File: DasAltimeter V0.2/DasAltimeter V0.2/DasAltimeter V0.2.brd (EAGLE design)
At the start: 38.9 x 21.6 mm, 53 parts, among them IC1 BMI055, U1 ATSAMD21G-A, U2 3.3V/150mA, U3 MS5803-14BA, U4 ADXL193, X1 22-23-2041, X2 22-23-2041

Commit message: playing with mini altimeter idea
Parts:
- removed C9: 0.1uF, SparkFun-Capacitors:0402
- removed H1: STAND-OFFTIGHT, SparkFun-Hardware:STAND-OFF-TIGHT
- removed R10, R14: 27k, SparkFun-Resistors:0402
- removed R11, R7: 100, SparkFun-Resistors:0402
- removed R12, R8: 3.3k, SparkFun-Resistors:0402
- removed R13, R9: 100k, SparkFun-Resistors:0402
- removed U$3: SI7232DN, SaL-lib1:SI7232DN
- removed U1: ATSAMD21G-A, SparkFun-IC-Microcontroller:TQFP-48
- removed U3: MS5803-14BA, SparkFun-Sensors:MS5803
- removed U4: ADXL193, SparkFun-Sensors:LCC-8
- removed X1: 22-23-2041, con-molex:22-23-2041
- added U$2: ATSAMD10D, SaL-lib1:ATSAMD10D
- added U$5: SIMPLE-MS5607, MS5607:MS5607
- C3: value 0.1uF -> 100nF
- C5: value 0.1uF -> 4.7uF
- moved X2 25.8 mm to (10.9, -7.49), turned to 0 degrees
- moved R2 24.8 mm to (21.2, -9.14), flipped to the bottom
- moved D2 22.8 mm to (22.9, -8.13)
- moved R17 22.2 mm to (13.8, -5.33), turned to 0 degrees
- moved R21 22.0 mm to (8.08, -5.33), turned to 0 degrees
- moved R4 21.7 mm to (24.1, -2.79), flipped to the bottom, turned to 0 degrees
- moved MEM 21.0 mm to (25.8, -3.05), turned to 0 degrees
- moved R5 20.8 mm to (26.5, 0.76), turned to 90 degrees
- moved C1 20.1 mm to (6.10, 2.16)
- moved C2 19.7 mm to (10.9, 2.03)
- moved U2 19.5 mm to (8.51, 2.16)
- moved C4 19.5 mm to (19.1, -3.81), turned to 0 degrees
- moved R18 19.4 mm to (13.8, -3.81), turned to 180 degrees
- moved R22 19.2 mm to (8.08, -3.81), turned to 180 degrees
- moved C8 18.6 mm to (33.4, -3.30)
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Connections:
- removed net FET_C: R9.1, U$3.7, U$3.8, U$3.9, X1.2
- removed net FET_D: R13.2, U$3.10, U$3.5, U$3.6, X1.3
- removed net FIRE_C: R7.2, R8.1, U1.34
- removed net FIRE_D: R11.1, R12.2, U1.33
- removed net N$3: C4.1, U1.43
- removed net N$8: R11.2, U$3.4
- removed net SENSE_C: R10.1, R9.2, U1.4
- removed net SENSE_D: R13.1, R14.2, U1.3
- removed net SPI0_MISO: IC1.10, IC1.15, U1.16
- removed net SPI0_MOSI: IC1.9, U1.13
- removed net SPI0_SCK: IC1.8, U1.14
- removed net SPI2_MISO: U1.22, U3.8
- removed net SPI2_MOSI: U1.21, U3.7
- removed net SPI2_SCK: U1.24, U3.1
- net !RESET: now also U$2.18; no longer U1.40
- net 3.3V: now also C4.1; no longer C3.1, C9.1, U1.17, U1.36, U1.44, U3.5, U4.P$7, U4.P$8
- net ACCELX: now also U$2.6; no longer U1.12, U4.P$6
- net BUZZER: now also U$2.10; no longer U1.30
- net CS_ACCEL: now also U$2.11; no longer U1.19
- net CS_BARO: now also U$2.17, U$5.5; no longer U1.23, U3.3
- net CS_GYRO: now also U$2.12; no longer U1.15
- net CS_MEM: now also U$2.13; no longer U1.27
- net FIRE_A: now also U$2.8; no longer U1.38
- net FIRE_B: now also U$2.7; no longer U1.37
- net GND: now also U$2.23, U$5.3; no longer C4.2, C9.2, R10.2, R12.1, R14.1, R8.2, U$3.1, U$3.3, U1.18, U1.35, U1.42, U1.5, U3.2, U3.6, U4.P$3
- net LED: now also U$2.9; no longer U1.29
- net N$1: now also C4.2, U$5.1; no longer R7.1, U$3.2
- net N$4: now also C3.1, U$2.24; no longer U1.6
- net RX: now also U$2.22; no longer U1.32
- net SENSE_A: now also U$2.1; no longer U1.48
- net SENSE_B: now also U$2.2; no longer U1.47
- net SENSE_BAT: now also U$2.5; no longer U1.11
- net SPI1_MISO: now also IC1.10, IC1.15, U$2.14; no longer U1.28
- net SPI1_MOSI: now also IC1.9, U$2.15; no longer U1.25
- net SPI1_SCK: now also IC1.8, U$2.16; no longer U1.26
- net SWCLK: now also U$2.19; no longer U1.45
- net SWDIO: now also U$2.20; no longer U1.46
- net TX: now also U$2.21; no longer U1.31
- net VCC: no longer X1.1, X1.4
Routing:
- net FIRE_A: track 19.4 -> 0.00 mm, vias 2 -> 0
- net 3.3V: track 15.8 -> 0.00 mm
- net CS_BARO: track 14.7 -> 0.00 mm
- net CS_MEM: track 14.4 -> 0.00 mm, vias 2 -> 0
- net LED: track 14.3 -> 0.00 mm, vias 1 -> 0
- net SENSE_A: track 13.1 -> 0.00 mm, vias 2 -> 0
- net SENSE_D: track 13.1 -> 0.00 mm, vias 2 -> 0
- net !RESET: track 12.7 -> 0.00 mm, vias 1 -> 0
- net FIRE_B: track 12.4 -> 0.00 mm, vias 2 -> 0
- net SPI1_MISO: track 12.2 -> 0.00 mm
- net SPI0_MISO: track 11.1 -> 0.00 mm
- net SWDIO: track 10.8 -> 0.00 mm, vias 2 -> 0
- net CS_GYRO: track 10.6 -> 0.00 mm, vias 2 -> 0
- net SWCLK: track 10.2 -> 0.00 mm
- net CS_ACCEL: track 9.99 -> 0.00 mm, vias 2 -> 0
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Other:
- board size 38.9 x 21.6 mm -> 36.3 x 17.8 mm

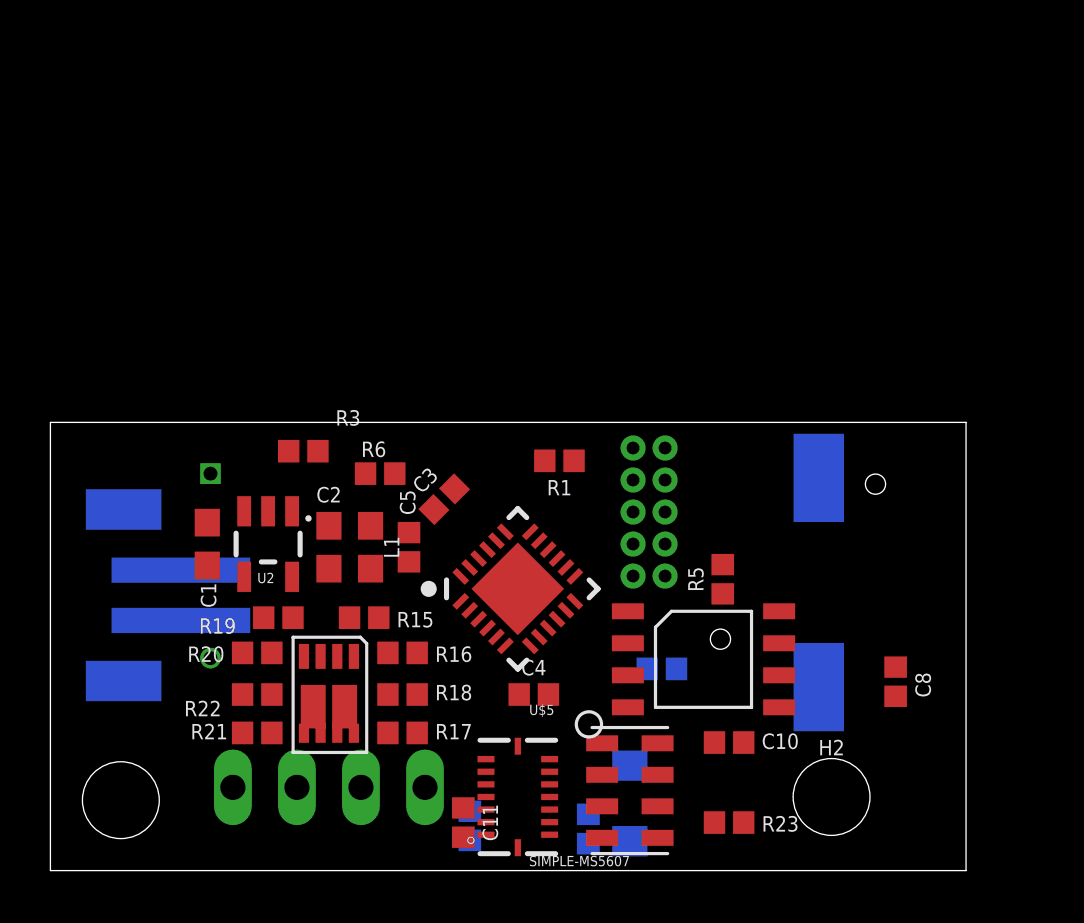
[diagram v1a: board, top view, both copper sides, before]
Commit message: Revert "playing with mini altimeter idea"
This reverts commit 0304c3ccd9bbc4967d121740b09f5fd7c2a4b911.
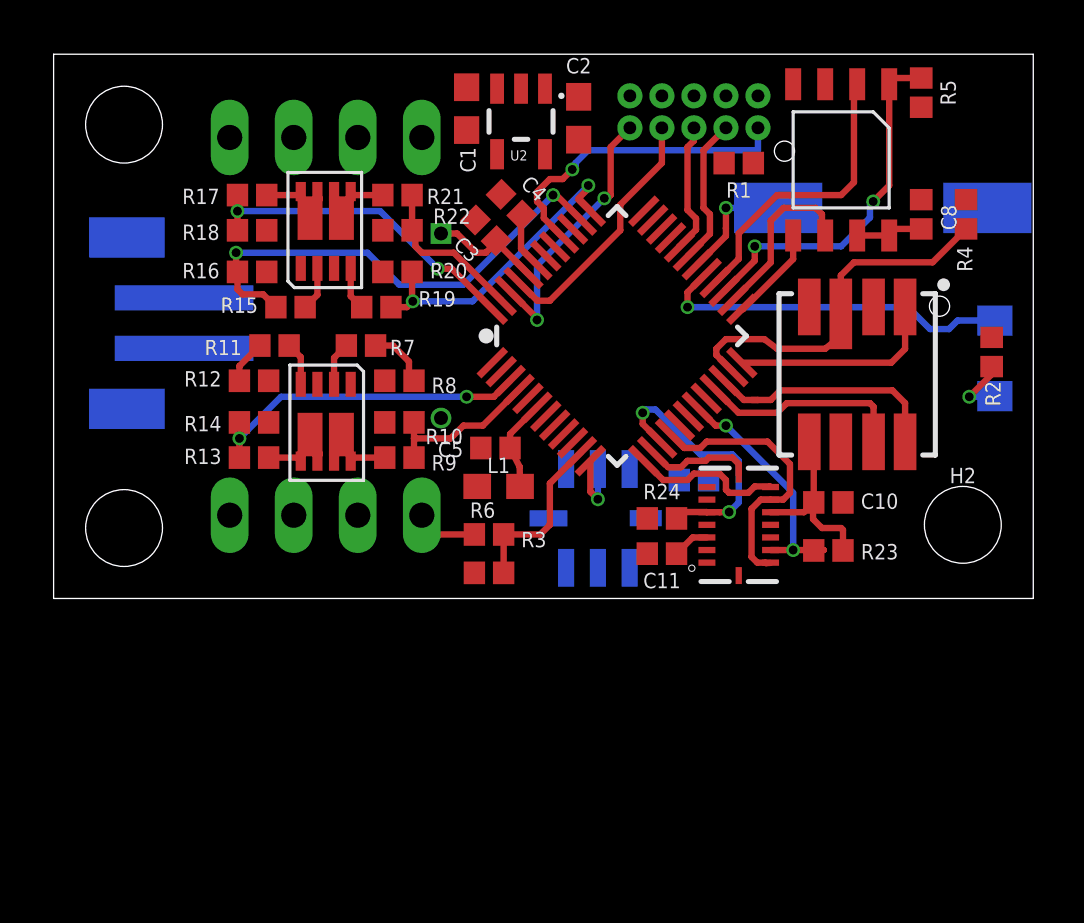
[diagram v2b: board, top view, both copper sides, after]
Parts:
- removed U$2: ATSAMD10D, SaL-lib1:ATSAMD10D
- removed U$5: SIMPLE-MS5607, MS5607:MS5607
- added C9: 0.1uF, SparkFun-Capacitors:0402
- added H1: STAND-OFFTIGHT, SparkFun-Hardware:STAND-OFF-TIGHT
- added R10, R14: 27k, SparkFun-Resistors:0402
- added R11, R7: 100, SparkFun-Resistors:0402
- added R12, R8: 3.3k, SparkFun-Resistors:0402
- added R13, R9: 100k, SparkFun-Resistors:0402
- added U$3: SI7232DN, SaL-lib1:SI7232DN
- added U1: ATSAMD21G-A, SparkFun-IC-Microcontroller:TQFP-48
- added U3: MS5803-14BA, SparkFun-Sensors:MS5803
- added U4: ADXL193, SparkFun-Sensors:LCC-8
- added X1: 22-23-2041, con-molex:22-23-2041
- C3: value 100nF -> 0.1uF
- C5: value 4.7uF -> 0.1uF
- moved X2 25.8 mm to (10.8, 18.3), turned to 180 degrees
- moved R2 24.8 mm to (37.2, 9.78), flipped to the top
- moved D2 22.8 mm to (37.3, 9.53)
- moved R17 22.2 mm to (7.87, 16.0), turned to 180 degrees
- moved R21 22.0 mm to (13.6, 16.0), turned to 180 degrees
- moved R4 21.7 mm to (36.2, 15.2), flipped to the top, turned to 90 degrees
- moved MEM 21.0 mm to (30.6, 17.4), turned to 270 degrees
- moved R5 20.8 mm to (34.4, 20.1), turned to 270 degrees
- moved C1 20.1 mm to (16.4, 19.4)
- moved C2 19.7 mm to (20.8, 19.1)
- moved U2 19.5 mm to (18.5, 18.9)
- moved C4 19.5 mm to (18.2, 15.6), turned to 135 degrees
- moved R18 19.4 mm to (7.87, 14.6), turned to 0 degrees
- moved R22 19.2 mm to (13.6, 14.6), turned to 0 degrees
- moved C8 18.6 mm to (34.4, 15.2)
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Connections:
- new net FET_C: R9.1, U$3.7, U$3.8, U$3.9, X1.2
- new net FET_D: R13.2, U$3.10, U$3.5, U$3.6, X1.3
- new net FIRE_C: R7.2, R8.1, U1.34
- new net FIRE_D: R11.1, R12.2, U1.33
- new net N$3: C4.1, U1.43
- new net N$8: R11.2, U$3.4
- new net SENSE_C: R10.1, R9.2, U1.4
- new net SENSE_D: R13.1, R14.2, U1.3
- new net SPI0_MISO: IC1.10, IC1.15, U1.16
- new net SPI0_MOSI: IC1.9, U1.13
- new net SPI0_SCK: IC1.8, U1.14
- new net SPI2_MISO: U1.22, U3.8
- new net SPI2_MOSI: U1.21, U3.7
- new net SPI2_SCK: U1.24, U3.1
- net !RESET: now also U1.40; no longer U$2.18
- net 3.3V: now also C3.1, C9.1, U1.17, U1.36, U1.44, U3.5, U4.P$7, U4.P$8; no longer C4.1
- net ACCELX: now also U1.12, U4.P$6; no longer U$2.6
- net BUZZER: now also U1.30; no longer U$2.10
- net CS_ACCEL: now also U1.19; no longer U$2.11
- net CS_BARO: now also U1.23, U3.3; no longer U$2.17, U$5.5
- net CS_GYRO: now also U1.15; no longer U$2.12
- net CS_MEM: now also U1.27; no longer U$2.13
- net FIRE_A: now also U1.38; no longer U$2.8
- net FIRE_B: now also U1.37; no longer U$2.7
- net GND: now also C4.2, C9.2, R10.2, R12.1, R14.1, R8.2, U$3.1, U$3.3, U1.18, U1.35, U1.42, U1.5, U3.2, U3.6, U4.P$3; no longer U$2.23, U$5.3
- net LED: now also U1.29; no longer U$2.9
- net N$1: now also R7.1, U$3.2; no longer C4.2, U$5.1
- net N$4: now also U1.6; no longer C3.1, U$2.24
- net RX: now also U1.32; no longer U$2.22
- net SENSE_A: now also U1.48; no longer U$2.1
- net SENSE_B: now also U1.47; no longer U$2.2
- net SENSE_BAT: now also U1.11; no longer U$2.5
- net SPI1_MISO: now also U1.28; no longer IC1.10, IC1.15, U$2.14
- net SPI1_MOSI: now also U1.25; no longer IC1.9, U$2.15
- net SPI1_SCK: now also U1.26; no longer IC1.8, U$2.16
- net SWCLK: now also U1.45; no longer U$2.19
- net SWDIO: now also U1.46; no longer U$2.20
- net TX: now also U1.31; no longer U$2.21
- net VCC: now also X1.1, X1.4
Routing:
- net FIRE_A: track 0.00 -> 19.4 mm, vias 0 -> 2
- net 3.3V: track 0.00 -> 15.8 mm
- net CS_BARO: track 0.00 -> 14.7 mm
- net CS_MEM: track 0.00 -> 14.4 mm, vias 0 -> 2
- net LED: track 0.00 -> 14.3 mm, vias 0 -> 1
- net SENSE_A: track 0.00 -> 13.1 mm, vias 0 -> 2
- net SENSE_D: track 0.00 -> 13.1 mm, vias 0 -> 2
- net !RESET: track 0.00 -> 12.7 mm, vias 0 -> 1
- net FIRE_B: track 0.00 -> 12.4 mm, vias 0 -> 2
- net SPI1_MISO: track 0.00 -> 12.2 mm
- net SPI0_MISO: track 0.00 -> 11.1 mm
- net SWDIO: track 0.00 -> 10.8 mm, vias 0 -> 2
- net CS_GYRO: track 0.00 -> 10.6 mm, vias 0 -> 2
- net SWCLK: track 0.00 -> 10.2 mm
- net CS_ACCEL: track 0.00 -> 9.99 mm, vias 0 -> 2
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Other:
- board size 36.3 x 17.8 mm -> 38.9 x 21.6 mm
